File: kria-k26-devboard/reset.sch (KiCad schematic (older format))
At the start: 32 parts, among them Q8 BSS138-7-F, U29 SN74AVC4T245PWR, U30 SN74AVC4T245PWR, U31 TPS3840PH30DBVR, U32 TPS3840PH30DBVR, U33 74LV07ATPWJ

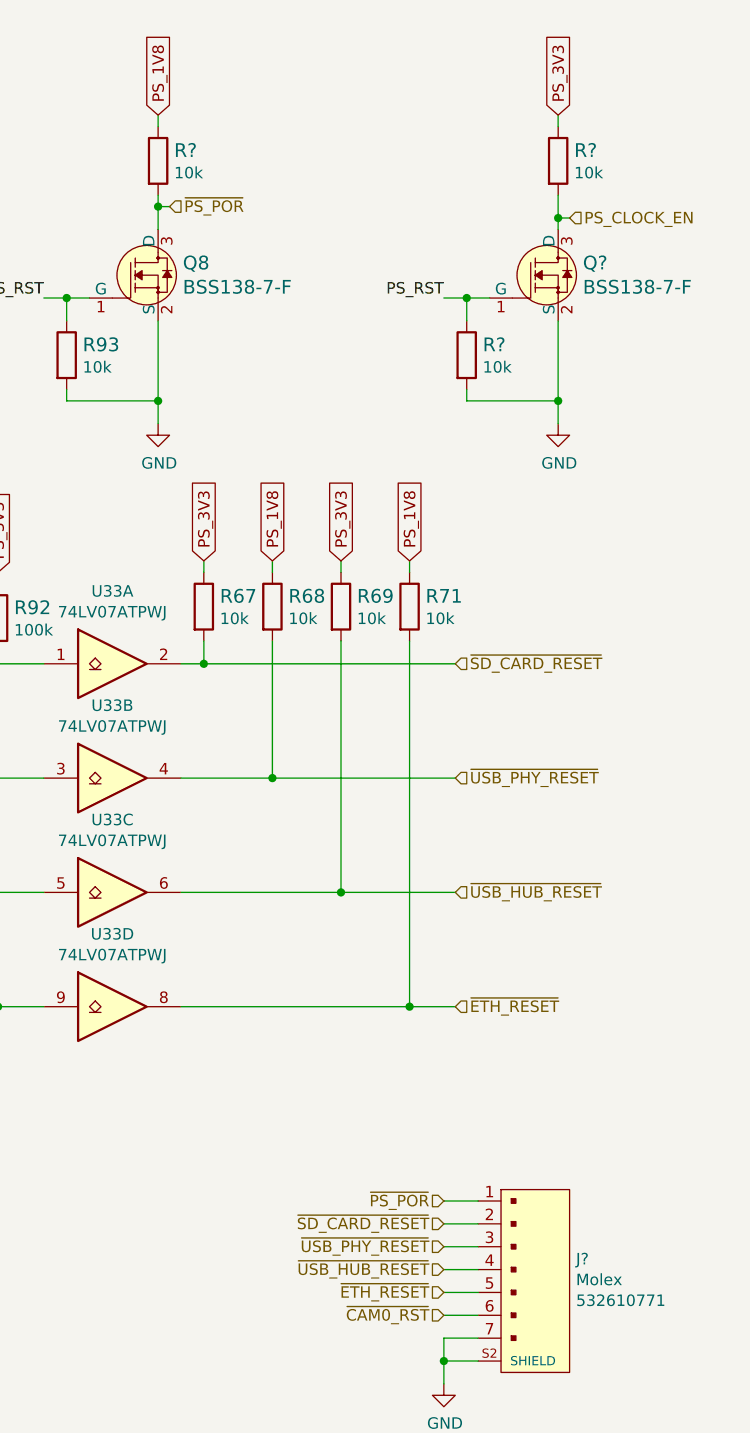
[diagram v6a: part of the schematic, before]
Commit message: Added Led voltage indicator, fan circuit. Tidied up supply and SOM sheet
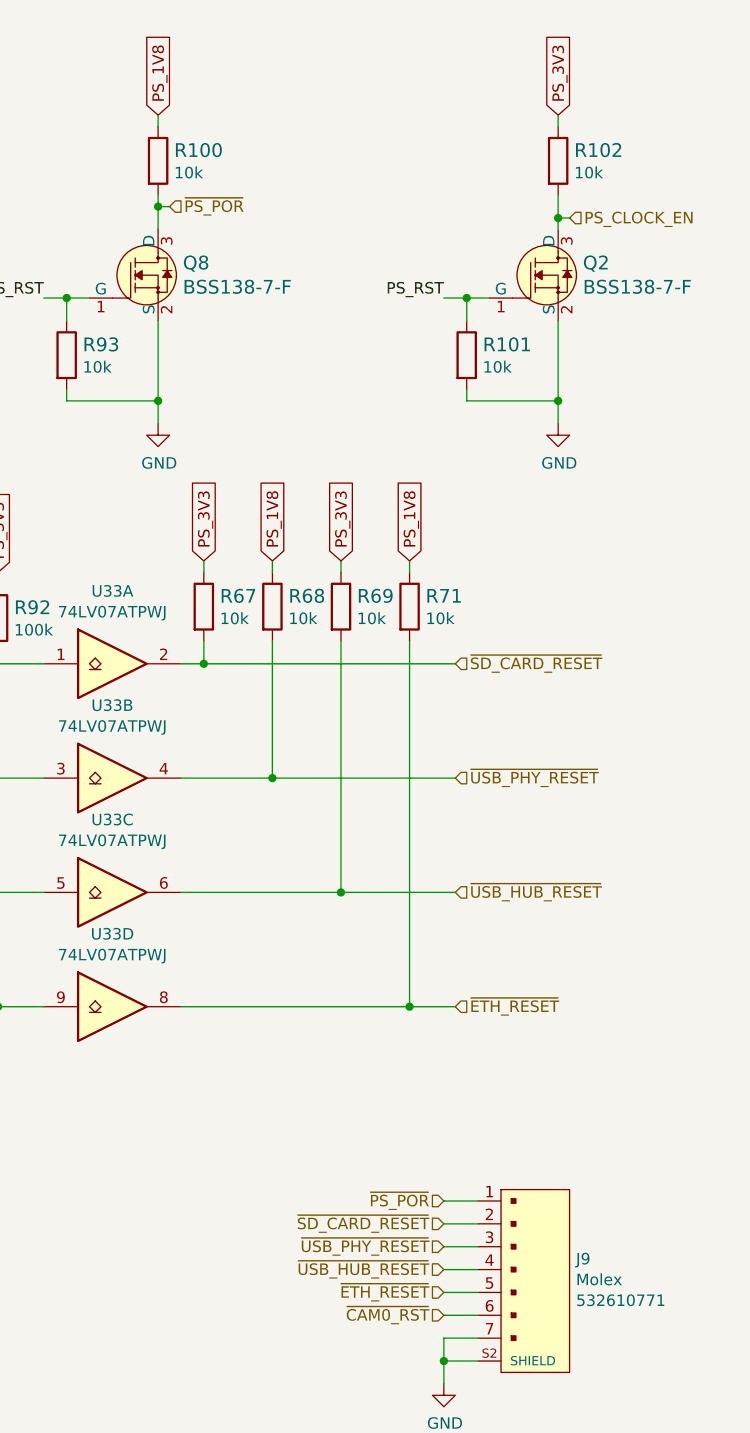
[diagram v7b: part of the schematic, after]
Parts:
- gave numbers to parts that had none: 5
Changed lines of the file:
@@
 25ms delay
 $Comp
-L antmicroRectangularConnectorsHeadersMalePins:532610771 J?
+L antmicroRectangularConnectorsHeadersMalePins:532610771 J9
 U 1 1 6252DE32
 P 11750 6050
-F 0 "J?" H 12078 6146 50  0000 L CNN
+F 0 "J9" H 12078 6146 50  0000 L CNN
 F 1 "532610771" H 11700 5550 50  0001 L BNN
 F 2 "antmicro-footprints:MOLEX_532610771" H 11750 6050 50  0001 L BNN
@@
 ~PS_POR
 $Comp
-L power:GND #PWR?
+L power:GND #PWR0346
 U 1 1 6253AB9B
 P 11500 6500
-F 0 "#PWR?" H 11500 6250 50  0001 C CNN
+F 0 "#PWR0346" H 11500 6250 50  0001 C CNN
 F 1 "GND" H 11505 6327 50  0000 C CNN
 F 2 "" H 11500 6500 50  0001 C CNN
@@
 PL_3V3
 $Comp
-L antmicroTransistorsFETsMOSFETsSingle:BSS138-7-F Q?
+L antmicroTransistorsFETsMOSFETsSingle:BSS138-7-F Q2
 U 1 1 625BE7A7
 P 12000 1650
-F 0 "Q?" H 12108 1703 60  0000 L CNN
+F 0 "Q2" H 12108 1703 60  0000 L CNN
 F 1 "BSS138-7-F" H 12108 1597 60  0000 L CNN
 F 2 "antmicro-footprints:SOT-23-3" H 12200 1850 60  0001 L CNN
@@
 	11500 1750 11600 1750
 $Comp
-L power:GND #PWR?
+L power:GND #PWR0347
 U 1 1 625BEA6D
 P 12000 2300
-F 0 "#PWR?" H 12000 2050 50  0001 C CNN
+F 0 "#PWR0347" H 12000 2050 50  0001 C CNN
 F 1 "GND" H 12005 2127 50  0000 C CNN
 F 2 "" H 12000 2300 50  0001 C CNN
@@
 PS_CLOCK_EN
 $Comp
-L antmicroResistors0402:R_10k_0402 R?
+L antmicroResistors0402:R_10k_0402 R101
 U 1 1 625BEA7D
 P 11600 2000
-F 0 "R?" V 11555 2070 60  0000 L CNN
+F 0 "R101" V 11555 2070 60  0000 L CNN
 F 1 "R_10k_0402" H 11600 1850 60  0001 C CNN
 F 2 "antmicro-footprints:0402-res" H 11800 2200 60  0001 L CNN
@@
 	12000 1000 12000 950
 $Comp
-L antmicroResistors0402:R_10k_0402 R?
+L antmicroResistors0402:R_10k_0402 R102
 U 1 1 625CF94D
 P 12000 1150
-F 0 "R?" V 11955 1220 60  0000 L CNN
+F 0 "R102" V 11955 1220 60  0000 L CNN
 F 1 "R_10k_0402" H 12000 1000 60  0001 C CNN
 F 2 "antmicro-footprints:0402-res" H 12200 1350 60  0001 L CNN
@@
 PS_1V8
 $Comp
-L antmicroResistors0402:R_10k_0402 R?
+L antmicroResistors0402:R_10k_0402 R100
 U 1 1 62627E6D
 P 10250 1150
-F 0 "R?" V 10205 1220 60  0000 L CNN
+F 0 "R100" V 10205 1220 60  0000 L CNN
 F 1 "R_10k_0402" H 10250 1000 60  0001 C CNN
 F 2 "antmicro-footprints:0402-res" H 10450 1350 60  0001 L CNN

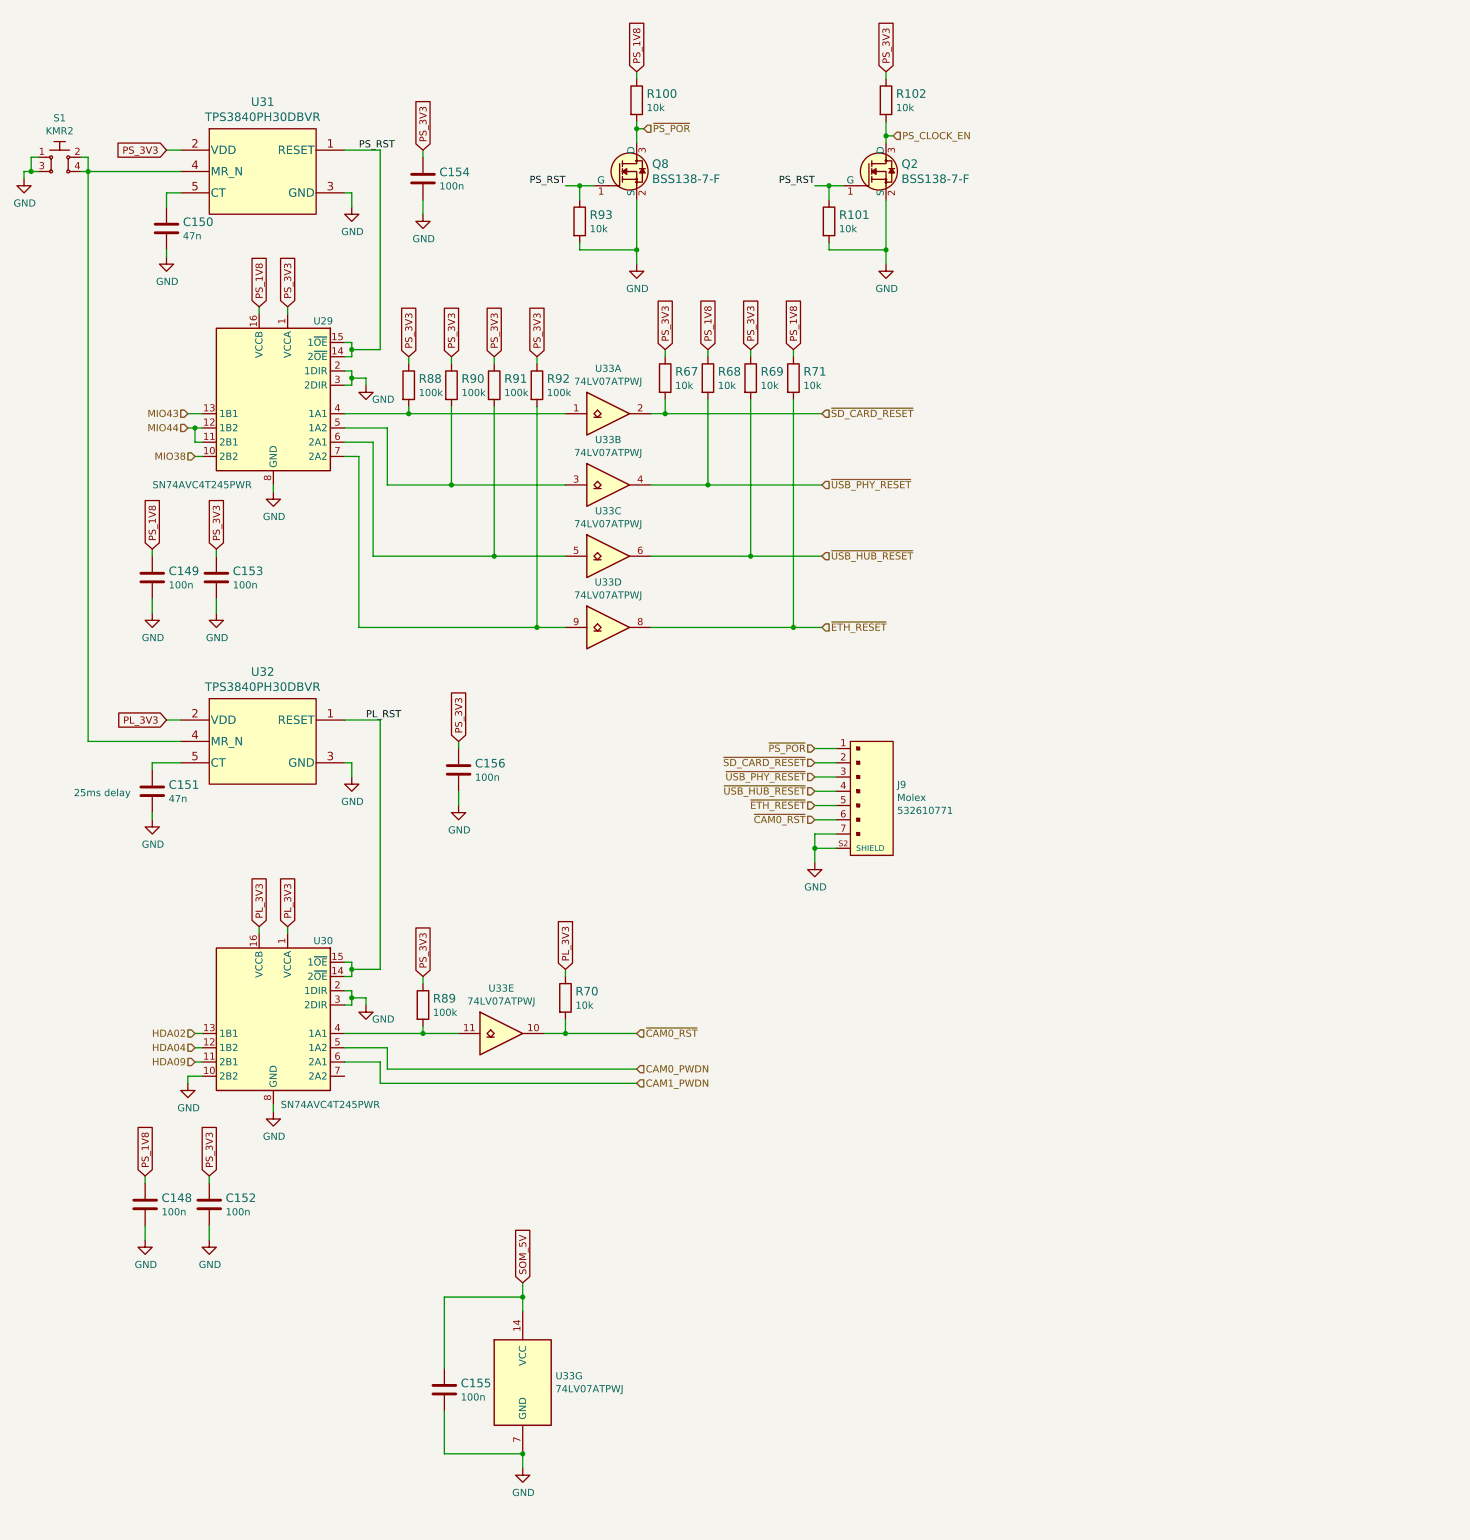
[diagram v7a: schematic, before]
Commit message: fixed an issue with reset logic (Mixed PS and PL domain on OD buffer), extended the logic circuit to support M.2 PERST# (reset for PCIe WIFI), fixed the polarity of the camera control signal CAM_RST to comply with Antmicro standard, change CAM _SHDN to CAM_VSYNC, replaced the reset connector to fit additional signal M2_PERST
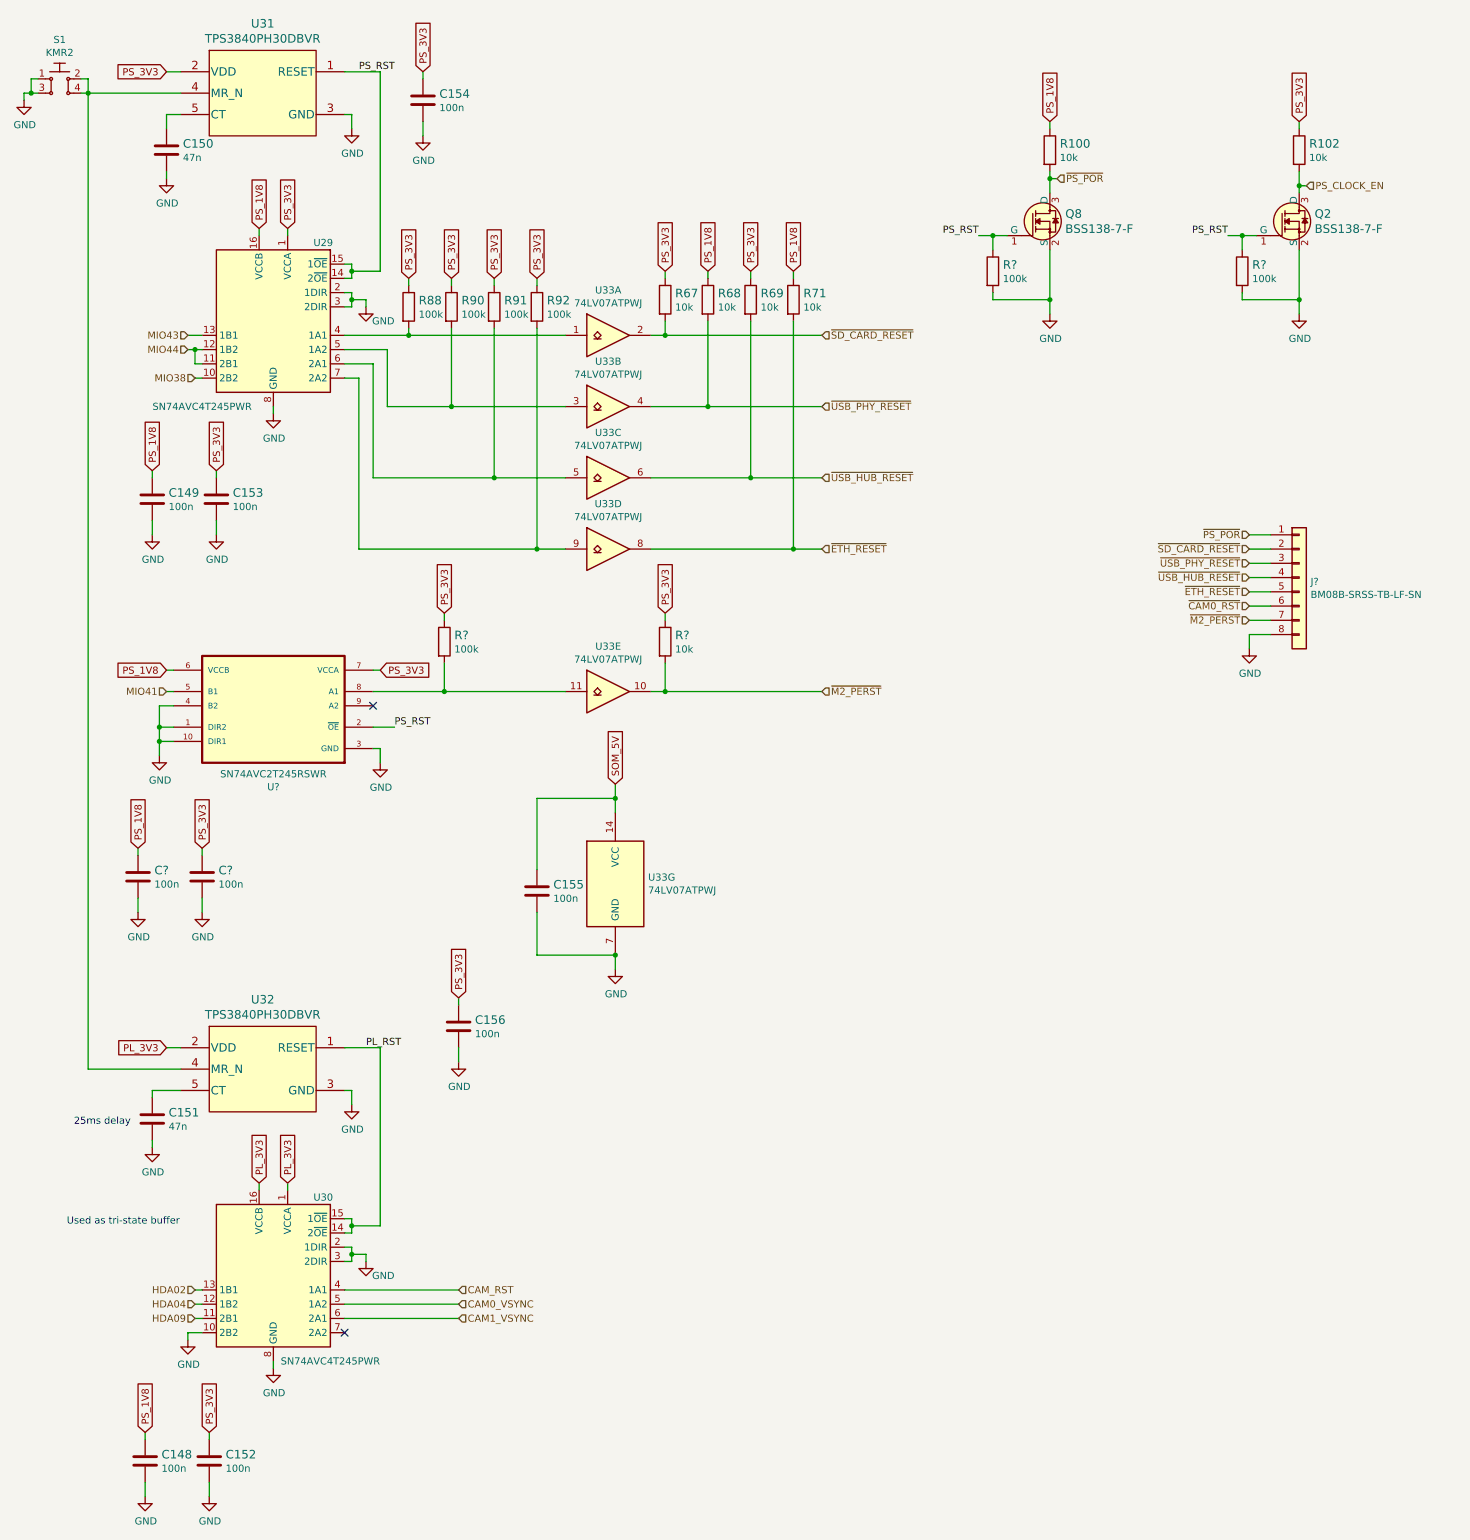
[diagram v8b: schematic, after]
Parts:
- removed J9: 532610771, antmicro-footprints:MOLEX_532610771, symbol antmicroRectangularConnectorsHeadersMalePins:532610771
- removed R101, R70, R93: R_10k_0402, antmicro-footprints:0402-res, symbol antmicroResistors0402:R_10k_0402
- removed R89: R_100k_0402, antmicro-footprints:0402-res, symbol antmicroResistors0402:R_100k_0402
- added C? (x2): C_100n_0402, antmicro-footprints:0402-cap, symbol antmicroCapacitors0402:C_100n_0402
- added J?: BM08B-SRSS-TB-LF-SN, antmicro-footprints:BM08B-SRSS-TB-LF-SN, symbol antmicroRectangularConnectorsHeadersMalePins:BM08B-SRSS-TB-LF-SN
- added R? (x3): R_100k_0402, antmicro-footprints:0402-res, symbol antmicroResistors0402:R_100k_0402
- added R?: R_10k_0402, antmicro-footprints:0402-res, symbol antmicroResistors0402:R_10k_0402
- added U?: SN74AVC2T245RSWR, antmicro-footprints:Texas_RSW0010A, symbol antmicroLogicTranslatorsLevelShifters:SN74AVC2T245RSWR
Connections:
- net GND: now also C?.2, C?.2, J?.8 (Pin_8), R?.2, R?.2, U?.1 (DIR2), U?.10 (DIR1), U?.3 (GND), U?.4 (B2)
- net PS_1V8: now also C?.1, U?.6 (VCCB)
- net PS_3V3: now also C?.1, R?.1, R?.1, U?.7 (VCCA)
- net PS_RST: now also R?.1, R?.1, U?.2 (~OE)
- net ~CAM0_RST: now also J?.6 (Pin_6); no longer U33.10
- net ~ETH_RESET: now also J?.5 (Pin_5)
- net ~PS_POR: now also J?.1 (Pin_1)
- net ~SD_CARD_RESET: now also J?.2 (Pin_2)
- net ~USB_HUB_RESET: now also J?.4 (Pin_4)
- net ~USB_PHY_RESET: now also J?.3 (Pin_3)
- net at U33.11: now also R?.2, U?.8 (A1); no longer U30.4 (1A1)
- net CAM0_PWDN renamed CAM0_VSYNC
- net CAM1_PWDN renamed CAM1_VSYNC
- new net CAM_RST: U30.4 (1A1)
- new net MIO41: U?.5 (B1)
- new net ~M2_PERST: J?.7 (Pin_7), R?.2, U33.10
- no-connect marks 0 -> 2
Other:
- note added: "Used as tri-state buffer"
- moved on the sheet: C148, C149, C150, C151, C152, C153, C154, C155, C156, Q2, Q8, R100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
